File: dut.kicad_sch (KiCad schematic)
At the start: 94 parts, among them J10 Conn_01x20, J11 Conn_01x20, J12 Conn_01x20, J15 Conn_01x20, J2 Conn_01x08, J4 Conn_01x10, J5 Conn_01x20, J6 Conn_01x20, J7 Conn_01x20, J8 Conn_01x02, J9 Conn_01x06, U11 MT9700_SY6280

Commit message: more routing
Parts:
- J15: footprint Connector_PinHeader_2.54mm:PinHeader_1x20_P2.54mm_Vertical -> Connector_PinHeader_2.54mm:PinHeader_1x19_P2.54mm_Vertical
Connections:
- net T10: no longer J8.1 (Pin_1)
- net T10i: now also J8.1 (Pin_1)
- net T11: no longer J8.2 (Pin_2)
- net T11i: now also J8.2 (Pin_2)
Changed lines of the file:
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@@
 	(wire
 		(pts
-			(xy 90.17 48.26) (xy 90.17 58.42)
+			(xy 105.41 110.49) (xy 105.41 118.11)
 		)
 		(stroke
@@
 	(wire
 		(pts
-			(xy 36.83 130.81) (xy 36.83 133.35)
+			(xy 90.17 48.26) (xy 90.17 58.42)
 		)
 		(stroke
@@
 	(wire
 		(pts
-			(xy 107.95 110.49) (xy 107.95 132.08)
+			(xy 36.83 130.81) (xy 36.83 133.35)
 		)
 		(stroke
@@
 	(wire
 		(pts
+			(xy 107.95 110.49) (xy 107.95 118.11)
+		)
+		(stroke
+			(width 0)
+			(type default)
+		)
+	)
+	(wire
+		(pts
 			(xy 85.09 143.51) (xy 85.09 152.4)
 		)
@@
 	(wire
 		(pts
-			(xy 105.41 110.49) (xy 105.41 132.08)
-		)
-		(stroke
-			(width 0)
-			(type default)
-		)
-	)
-	(wire
-		(pts
 			(xy 105.41 69.85) (xy 105.41 80.01)
 		)
@@
 		)
 	)
-	(label "ARDUINO_RESET"
+	(label "T11i"
 		(at 54.61 185.42 0)
 		(effects
@@
 		)
 	)
-	(label "ARDUINO_RESET"
-		(at 107.95 132.08 0)
-		(effects
-			(font
-				(size 1.27 1.27)
-			)
-			(justify left bottom)
-		)
-	)
 	(label "B18i"
 		(at 125.73 161.29 90)
@@
 		)
 	)
-	(label "ARDUINO_IOREF"
+	(label "T10i"
 		(at 52.07 185.42 180)
 		(effects
@@
 		)
 	)
-	(label "ARDUINO_IOREF"
-		(at 105.41 132.08 180)
-		(effects
-			(font
-				(size 1.27 1.27)
-			)
-			(justify right bottom)
-		)
-	)
 	(label "B10i"
 		(at 36.83 138.43 270)
@@
 			)
 		)
-		(property "Footprint" "Connector_PinHeader_2.54mm:PinHeader_1x20_P2.54mm_Vertical"
+		(property "Footprint" "Connector_PinHeader_2.54mm:PinHeader_1x19_P2.54mm_Vertical"
 			(at 105.41 95.25 0)
 			(hide yes)

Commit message: Start v2
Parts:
- removed C58, C59: 10uF, Capacitor_SMD:C_0603_1608Metric, symbol Device:C_Small
- removed R71, R72: 10K, Resistor_SMD:R_0402_1005Metric, symbol Device:R_Small
- removed U11: MT9700_SY6280, Package_TO_SOT_SMD:SOT-23-5, symbol GenericJLC:MT9700_SY6280
- added C60, C61, C62: 0.1uF, Capacitor_SMD:C_0402_1005Metric, symbol Device:C_Small
- added J20: Conn_02x04_Odd_Even, Connector_PinHeader_2.54mm:PinHeader_2x04_P2.54mm_Vertical, symbol Connector_Generic:Conn_02x04_Odd_Even
- added PORT5: LED_Small, LED_SMD:LED_0603_1608Metric, symbol Device:LED_Small
- added R73: 4.7K, Resistor_SMD:R_0402_1005Metric, symbol Device:R_Small
- added U11, U12, U5: PI4IOE5V9535ZDEX, Package_DFN_QFN:VQFN-24-1EP_4x4mm_P0.5mm_EP2.45x2.45mm, symbol Interface_Expansion:TCA9535RGER
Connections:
- net +3.3V: now also C60.1, C61.1, C62.1, PORT5.2 (A), U11.21 (VCC), U11.24 (A2), U12.21 (VCC), U12.23 (A1), U12.24 (A2), U5.21 (VCC)
- net GND: now also C60.2, C61.2, C62.2, U11.18 (A0), U11.23 (A1), U11.25 (EPAD), U11.9 (GND), U12.18 (A0), U12.25 (EPAD), U12.9 (GND), U5.18 (A0), U5.23 (A1), U5.24 (A2), U5.25 (EPAD), U5.9 (GND)
- removed net I2C_PULL_UP: R100.1, R101.1, R102.1, R103.1, R104.1, R105.1, R106.1, R107.1, R108.1, R109.1, R110.1, R111.1, R112.1, R113.1, R74.1, R75.1, R76.1, R77.1, R78.1, R79.1, R80.1, R81.1, R82.1, R83.1, R84.1, R85.1, R86.1, R87.1, R88.1, R89.1, R90.1, R91.1, R92.1, R94.1, R95.1, R96.1, R97.1, R98.1, R99.1
- new net: R79.1, U12.4 (P03)
- new net: R113.1, U11.15 (P15)
- new net: R85.1, U11.1 (P00)
- new net: R101.1, U12.5 (P04)
- new net: R80.1, U12.6 (P05)
- new net: R88.1, U11.7 (P06)
- new net: R111.1, U11.11 (P11)
- new net: R89.1, U11.10 (P10)
- new net: R96.1, U5.11 (P11)
- new net: R76.1, U5.14 (P14)
- new net: PORT5.1 (K), R73.1
- new net: R95.1, U5.8 (P07)
- new net: R107.1, U11.2 (P01)
- new net: R103.1, U12.10 (P10)
- new net: R91.1, U11.14 (P14)
- new net: R100.1, U12.3 (P02)
- new net: R86.1, U11.3 (P02)
- new net: R84.1, U12.15 (P15)
- new net: R99.1, U12.1 (P00)
- new net: R82.1, U12.11 (P11)
- new net: R104.1, U12.12 (P12)
- new net: R83.1, U12.13 (P13)
- new net: R105.1, U12.14 (P14)
- new net: R106.1, U12.16 (P16)
- new net: R78.1, U12.2 (P01)
- new net: R102.1, U12.7 (P06)
- new net: R81.1, U12.8 (P07)
- new net: R74.1, U5.10 (P10)
- new net: R75.1, U5.12 (P12)
- new net: R97.1, U5.13 (P13)
- new net: R98.1, U5.15 (P15)
- new net: R77.1, U5.16 (P16)
- new net: R94.1, U5.7 (P06)
- new net: R90.1, U11.12 (P12)
- new net: R110.1, U11.8 (P07)
- new net: R112.1, U11.13 (P13)
- new net: R92.1, U11.16 (P16)
- new net: R108.1, U11.4 (P03)
- new net: R87.1, U11.5 (P04)
- new net: R109.1, U11.6 (P05)
- new net P06: R73.2
- new net P10: J20.7 (Pin_7)
- new net P11: J20.5 (Pin_5)
- new net P12: J20.8 (Pin_8)
- new net P13: J20.6 (Pin_6)
- new net P14: J20.3 (Pin_3)
- new net P15: J20.4 (Pin_4)
- new net P16: J20.1 (Pin_1)
- new net P17: J20.2 (Pin_2)
- new net SCL: U11.19 (SCL), U12.19 (SCL), U5.19 (SCL)
- new net SDA: U11.20 (SDA), U12.20 (SDA), U5.20 (SDA)
- no-connect marks 1 -> 4
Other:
- note removed: "6.8k/10k = 0.6A"
- moved on the sheet: R100, R101, R102, R103, R104, R105, R106, R107, R108, R109, R110, R111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

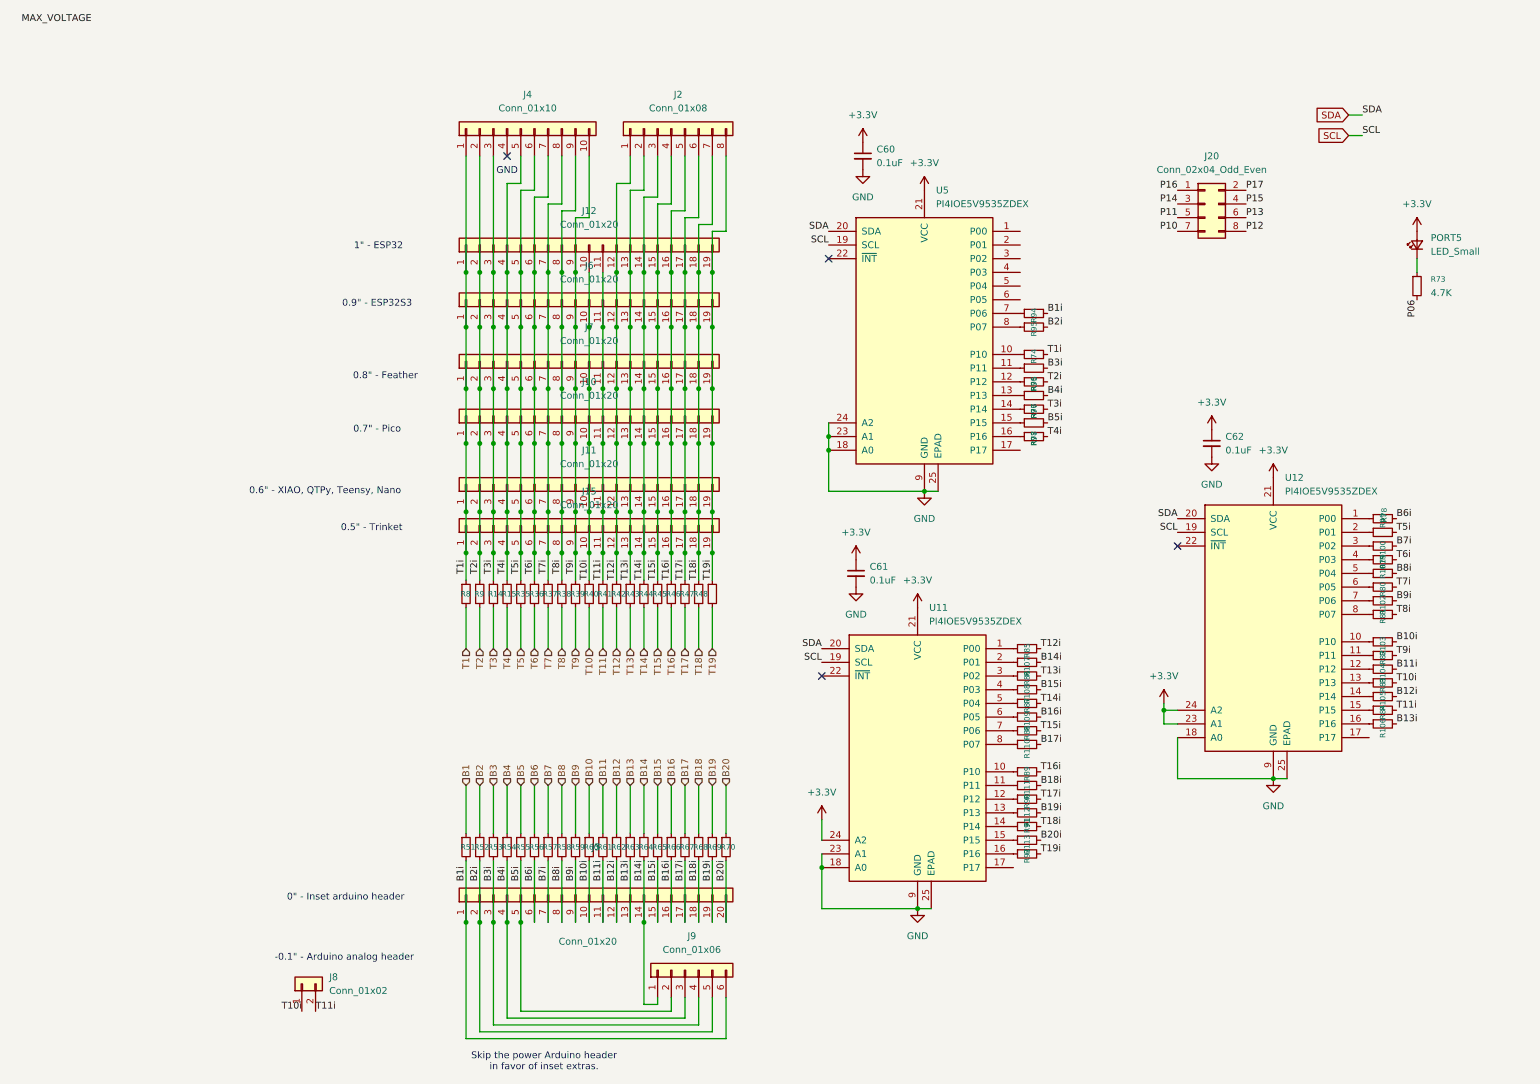
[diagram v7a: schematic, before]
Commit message: Add IO expanders, swap ethernet and move USB LEDs
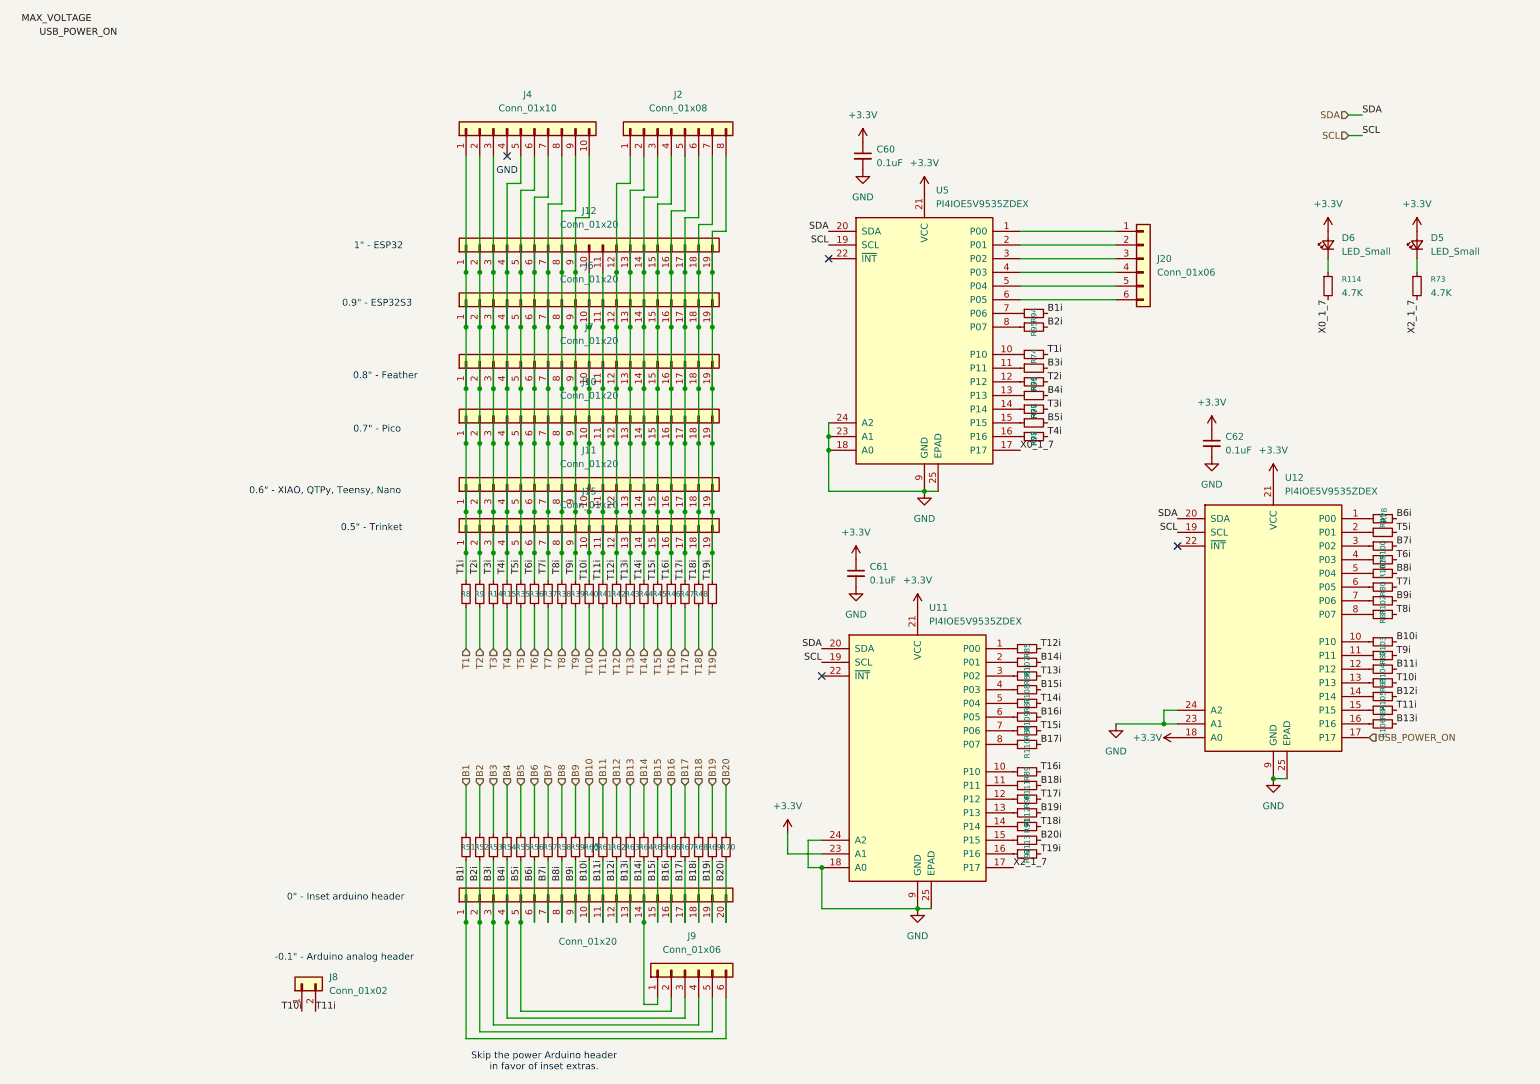
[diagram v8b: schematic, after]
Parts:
- removed J20: Conn_02x04_Odd_Even, Connector_PinHeader_2.54mm:PinHeader_2x04_P2.54mm_Vertical, symbol Connector_Generic:Conn_02x04_Odd_Even
- added D6: LED_Small, LED_SMD:LED_0603_1608Metric, symbol Device:LED_Small
- added J20: Conn_01x06, Connector_PinHeader_2.54mm:PinHeader_1x06_P2.54mm_Vertical, symbol Connector_Generic:Conn_01x06
- added R114: 4.7K, Resistor_SMD:R_0402_1005Metric, symbol Device:R_Small
- renumbered PORT5 to D5
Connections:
- net P06 is gone; now on net X2_1_7: R73.2
- net +3.3V: now also U11.23 (A1), U12.18 (A0), D6.2 (A); no longer U11.24 (A2), U12.23 (A1), U12.24 (A2)
- net GND: now also U11.24 (A2), U12.23 (A1), U12.24 (A2); no longer U11.23 (A1), U12.18 (A0)
- net USB_POWER_ON: now reaches U12.17 (P17)
- net at U5.1 (P00): now also J20.1 (Pin_1)
- net X0_1_7: now reaches U5.17 (P17)
- net X0_1_7: now also R114.2
- net at U5.2 (P01): now also J20.2 (Pin_2)
- net at U5.3 (P02): now also J20.3 (Pin_3)
- net at U5.4 (P03): now also J20.4 (Pin_4)
- net at U5.5 (P04): now also J20.5 (Pin_5)
- net at U5.6 (P05): now also J20.6 (Pin_6)
- net X2_1_7: now reaches U11.17 (P17)
- new net: D6.1 (K), R114.1
